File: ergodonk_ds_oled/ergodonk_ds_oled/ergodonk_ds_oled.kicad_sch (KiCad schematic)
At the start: 131 parts, among them J10 Pimaroni Trackball, J2 4PIN, Q1 TIP120, SW08_RH10 SW_PUSH_LED, SW1 SW_PUSH_LED, SW10 SW_PUSH_LED, SW11 SW_PUSH_LED, SW12 SW_PUSH_LED, SW13 SW_PUSH_LED, SW14 SW_PUSH_LED, SW15 SW_PUSH_LED, SW16 SW_PUSH_LED, SW17 SW_PUSH_LED, SW18_RH10 SW_PUSH_LED, SW2 SW_PUSH_LED, SW20 SW_PUSH_LED, SW21 SW_PUSH_LED, SW22 SW_PUSH_LED, SW23 SW_PUSH_LED, SW24 SW_PUSH_LED, SW25 SW_PUSH_LED, SW26 SW_PUSH_LED, SW27 SW_PUSH_LED, SW28_RH10 SW_PUSH_LED, SW3 SW_PUSH_LED, SW30 SW_PUSH_LED, SW31 SW_PUSH_LED, SW32 SW_PUSH_LED, SW33 SW_PUSH_LED, SW34 SW_PUSH_LED, SW35 SW_PUSH_LED, SW36 SW_PUSH_LED, SW37 SW_PUSH_LED, SW38_RH10 SW_PUSH_LED, SW4 SW_PUSH_LED, SW40 SW_PUSH_LED, SW42 SW_PUSH_LED, SW43 SW_PUSH_LED, SW44 SW_PUSH_LED, SW45 SW_PUSH_LED, SW46 SW_PUSH_LED, SW47 SW_PUSH_LED, SW48_RH10 SW_PUSH_LED, SW5 SW_PUSH_LED, SW50 SW_PUSH_LED, SW51 SW_PUSH_LED, SW52 SW_PUSH_LED, SW53 SW_PUSH_LED, SW54 SW_PUSH_LED, SW55 SW_PUSH_LED, SW56 SW_PUSH_LED, SW57 SW_PUSH_LED, SW58 SW_PUSH_LED, SW6 SW_PUSH_LED, SW7 SW_PUSH_LED, U11 Pico

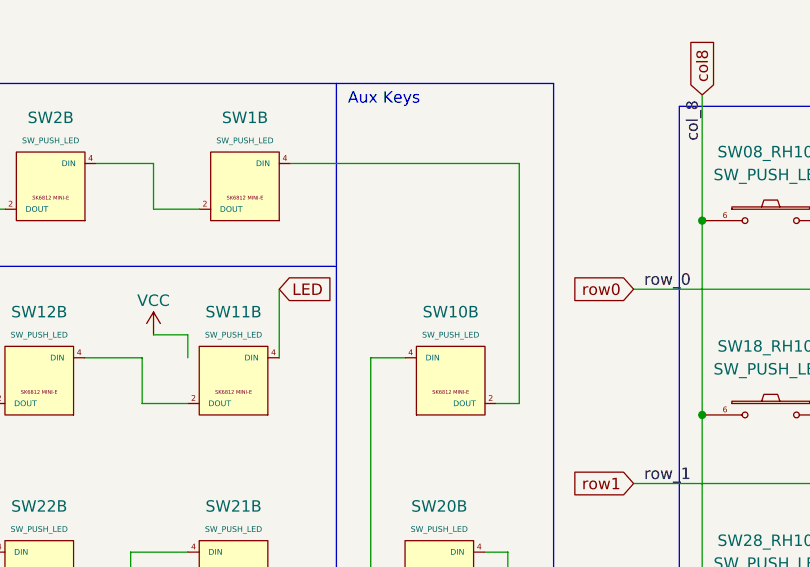
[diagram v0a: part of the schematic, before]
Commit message: Added 'simple' variant
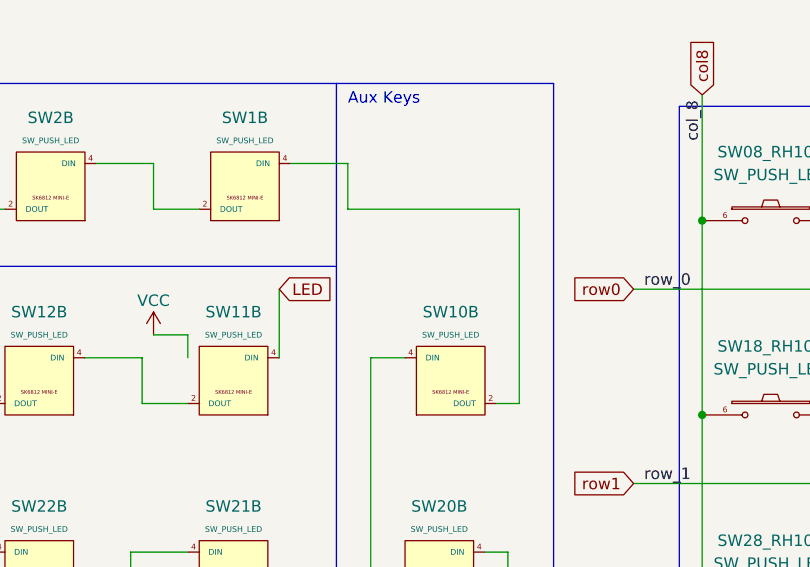
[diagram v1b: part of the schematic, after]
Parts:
- OL10: footprint ergodonk_kicad_library:OLED SSD1306 128x64 UNVERIFIED -> ergodonk_pico:OLED SSD1306 128x64 UNVERIFIED v2
- SW1, SW10, SW11, SW12, SW13, SW14, SW15, SW16, SW17, SW2, SW20, SW21, SW22, SW23, SW24, SW25, SW26, SW3, SW30, SW31, SW32, SW33, SW34, SW35, SW36, SW4, SW40, SW42, SW43, SW44, SW45, SW46, SW5, SW50, SW54, SW55, SW56, SW6, SW7: footprint ergodonk_kicad_library:Cherry_MX_DS_Hotswap_miniE_1U_sofle3b -> ergodonk_pico:Cherry_MX_DS_Hotswap_miniE_1U_sofle3b v2
- SW51, SW52: footprint ergodonk_kicad_library:V2_CherryMX_DoubleSided_Hotswap_miniE_2u_Vertical -> ergodonk_pico:Cherry_MX_DS_Hotswap_miniE_1U_sofle3b v2
- SW53: footprint ergodonk_kicad_library:V2_CherryMX_DoubleSided_Hotswap_miniE_1.25u_Vertical -> ergodonk_pico:Cherry_MX_DS_Hotswap_miniE_1U_sofle3b v2
- SW57, SW58: footprint ergodonk_kicad_library:V2_CherryMX_DoubleSided_Hotswap_miniE_1.25u -> ergodonk_pico:Cherry_MX_DS_Hotswap_miniE_1U_sofle3b v2
